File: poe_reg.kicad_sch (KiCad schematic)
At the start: 29 parts, among them T2 POE30P-50L, U5 MP6004GQ-P

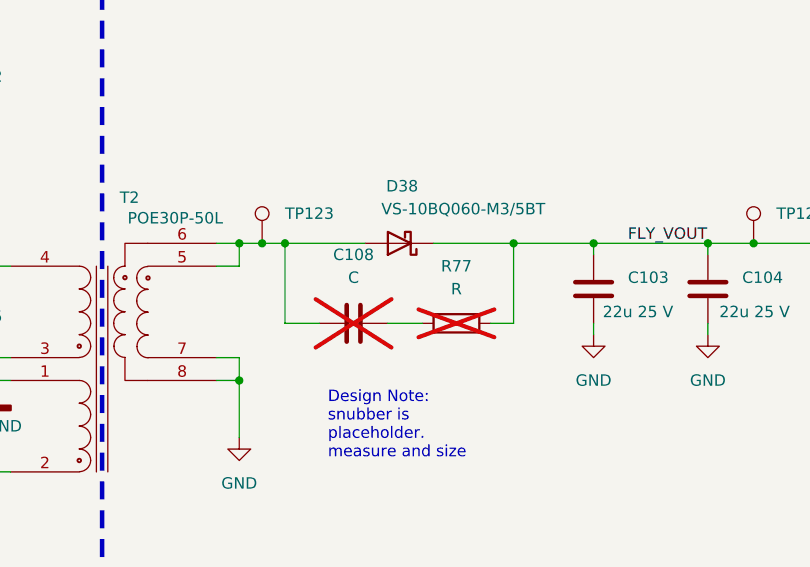
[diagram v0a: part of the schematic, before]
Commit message: did stuff, amongst others changed to op-amp input filter
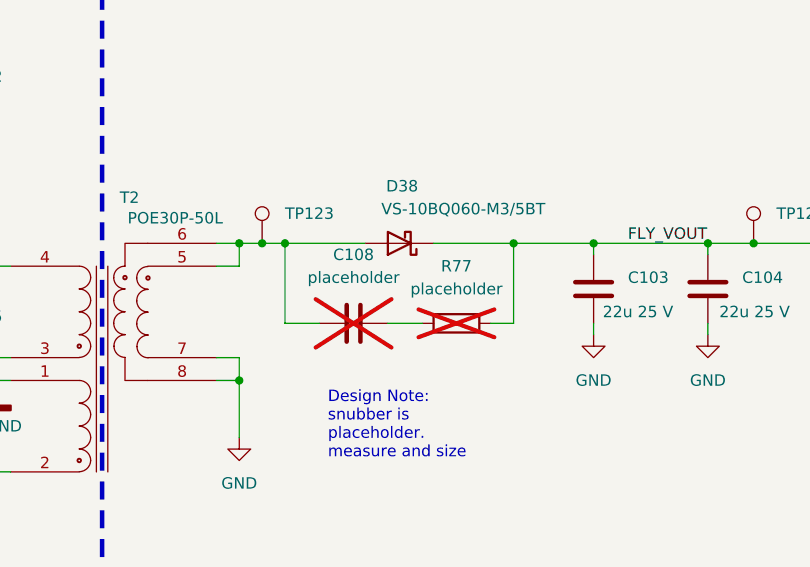
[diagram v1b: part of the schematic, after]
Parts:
- C108: value C -> placeholder
- D37: LCSC (none) -> C894760
- R77: value R -> placeholder

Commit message: did stuff
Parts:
- C102: LCSC (none) -> C2941944; LCSC Part (none) -> C2941944
- C106: LCSC (none) -> C170101; LCSC Basic/Pref (none) -> n; LCSC Part (none) -> C170101
- D80: value MMBZ5256ELT1G -> BZX84C30-7-F; LCSC (none) -> C151632; LCSC Basic/Pref (none) -> n; LCSC Part (none) -> C151632; LCSC missing x -> (none)
- R78: value 68k -> 150k; footprint Resistor_SMD:R_0402_1005Metric -> Resistor_SMD:R_0603_1608Metric; LCSC C36871 -> C22807; LCSC Part C36871 -> C22807
- R79: value 12k -> 24K; footprint Resistor_SMD:R_0402_1005Metric -> Resistor_SMD:R_0603_1608Metric; LCSC C25752 -> C23352; LCSC Part C25752 -> C23352
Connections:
- net +5.2V renamed +5.3V
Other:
- note removed: "TODO: Replace D80, not on LCSC"
- note removed: "TODO: recalc for 5.2 V"
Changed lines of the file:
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@@
 	(generator_version "10.0")
 	(paper "A3")
-	(text "TODO: recalc for 5.2 V"
+	(text "PoE Flyback Regulator"
 		(exclude_from_sim no)
-		(at 133.858 98.806 0)
+		(at 205.232 35.56 0)
 		(effects
 			(font
-				(size 1.27 1.27)
+				(size 12.7 12.7)
+				(thickness 1.5875)
 			)
 		)
 	)
-	(text "PoE Flyback Regulator"
+	(text "CAD Note:\n2kV isolation\n"
 		(exclude_from_sim no)
-		(at 150.622 25.4 0)
+		(at 210.312 92.456 0)
 		(effects
 			(font
-				(size 12.7 12.7)
-				(thickness 1.5875)
+				(size 1.27 1.27)
+				(color 255 0 3 1)
 			)
+			(justify left)
 		)
 	)
-	(text "TODO: Replace D80, not on LCSC"
+	(text_box "Design Note:\nD38 Vf = 0.42 V @ 1 A"
 		(exclude_from_sim no)
-		(at 76.454 120.396 0)
+		(at 260.35 113.03 0)
+		(size 26.67 5.9929)
+		(margins 0.9525 0.9525 0.9525 0.9525)
+		(stroke
+			(width -0.0001)
+			(type solid)
+		)
+		(fill
+			(type none)
+		)
 		(effects
 			(font
 				(size 1.27 1.27)
 			)
+			(justify left top)
 		)
 	)
-	(text "CAD Note:\n2kV isolation\n"
+	(text_box "Design Note:\n150k over 24k =>\n~5.321 V\nthere is significant inaccuracy\nworst case +/- ~0.5 V"
 		(exclude_from_sim no)
-		(at 210.312 92.456 0)
+		(at 180.34 177.8 0)
+		(size 27.94 20.3053)
+		(margins 0.9525 0.9525 0.9525 0.9525)
+		(stroke
+			(width -0.0001)
+			(type solid)
+		)
+		(fill
+			(type none)
+		)
 		(effects
 			(font
 				(size 1.27 1.27)
-				(color 255 0 3 1)
 			)
-			(justify left)
+			(justify left top)
 		)
 	)
@@
 		)
 	)
-	(text_box "Design Note:\nsnubber is placeholder.\nmeasure and size"
+	(text_box "Design Note:\nPOE30P-50L\n310uH (279uH Ipk)\n1.02 ohm pri 2.01 ohm bias 0.118 ohm sec\npri:sec = 1:0.28\npri:bias = 1:0.7"
 		(exclude_from_sim no)
-		(at 240.03 139.7 0)
-		(size 22.86 20.3053)
+		(at 220.98 96.52 0)
+		(size 45.72 14.1714)
 		(margins 0.9525 0.9525 0.9525 0.9525)
 		(stroke
@@
 		)
 	)
-	(text_box "Design Note:\nEN\n30 V Zener + 10k over 13k\n36.9 V rising\n32.3 V falling\n"
+	(text_box "Design Note:\nsnubber is placeholder.\nmeasure and size"
 		(exclude_from_sim no)
-		(at 68.58 156.21 0)
-		(size 22.86 14.1714)
+		(at 240.03 139.7 0)
+		(size 22.86 20.3053)
 		(margins 0.9525 0.9525 0.9525 0.9525)
 		(stroke
@@
 		)
 	)
-	(text_box "TODO:\nselect capacitors to chose footprints\n\nRCD diode"
+	(text_box "Design Note:\nEN\n30 V Zener + 10k over 13k\n36.9 V rising\n32.3 V falling\n"
 		(exclude_from_sim no)
-		(at 109.22 77.4847 0)
-		(size 22.86 20.3053)
+		(at 68.58 156.21 0)
+		(size 22.86 14.1714)
 		(margins 0.9525 0.9525 0.9525 0.9525)
 		(stroke
@@
 			)
 		)
-		(property "LCSC Basic/Pref" ""
+		(property "LCSC Basic/Pref" "n"
 			(at 124.46 115.57 0)
 			(hide yes)
@@
 			)
 		)
+		(property "LCSC" "C170101"
+			(at 124.46 115.57 0)
+			(hide yes)
+			(show_name no)
+			(do_not_autoplace no)
+			(effects
+				(font
+					(size 1.27 1.27)
+				)
+			)
+		)
+		(property "LCSC Part" "C170101"
+			(at 124.46 115.57 0)
+			(hide yes)
+			(show_name no)
+			(do_not_autoplace no)
+			(effects
+				(font
+					(size 1.27 1.27)
+				)
+			)
+		)
 		(pin "2"
 		)
@@
 			)
 		)
-		(property "Datasheet" "MP6004GQ-P"
+		(property "Datasheet" "https://www.monolithicpower.com/en/documentview/productdocument/index/version/2/document_type/Datasheet/lang/en/sku/MP6004/document_id/1864/"
 			(at 133.35 129.54 0)
 			(hide yes)
@@
 			)
 		)
+		(property "LCSC" "C2941944"
+			(at 190.5 114.3 0)
+			(hide yes)
+			(show_name no)
+			(do_not_autoplace no)
+			(effects
+				(font
+					(size 1.27 1.27)
+				)
+			)
+		)
+		(property "LCSC Part" "C2941944"
+			(at 190.5 114.3 0)
+			(hide yes)
+			(show_name no)
+			(do_not_autoplace no)
+			(effects
+				(font
+					(size 1.27 1.27)
+				)
+			)
+		)
 		(pin "2"
 		)
@@
 			)
 		)
-		(property "Value" "68k"
+		(property "Value" "150k"
 			(at 193.04 156.2099 0)
 			(show_name no)
@@
 			)
 		)
-		(property "Footprint" "Resistor_SMD:R_0402_1005Metric"
+		(property "Footprint" "Resistor_SMD:R_0603_1608Metric"
 			(at 188.722 154.94 90)
 			(hide yes)
@@
 			)
 		)
-		(property "LCSC" "C36871"
+		(property "LCSC" "C22807"
 			(at 190.5 154.94 0)
 			(hide yes)
@@
 			)
 		)
-		(property "LCSC Part" "C36871"
+		(property "LCSC Part" "C22807"
 			(at 190.5 154.94 0)
 			(hide yes)
@@
 			)
 		)
-		(property "Value" "MMBZ5256ELT1G"
+		(property "Value" "BZX84C30-7-F"
 			(at 77.724 129.032 90)
 			(show_name no)
@@
 			)
 		)
-		(property "LCSC Basic/Pref" ""
+		(property "LCSC Basic/Pref" "n"
 			(at 96.52 127 90)
 			(hide yes)
@@
 			)
 		)
-		(property "LCSC missing" "x"
+		(property "LCSC missing" ""
 			(at 96.52 127 90)
 			(hide yes)
@@
 			)
 		)
+		(property "LCSC" "C151632"
+			(at 96.52 127 90)
+			(hide yes)
+			(show_name no)
+			(do_not_autoplace no)
+			(effects
+				(font
+					(size 1.27 1.27)
+				)
+			)
+		)
+		(property "LCSC Part" "C151632"
+			(at 96.52 127 90)
+			(hide yes)
+			(show_name no)
+			(do_not_autoplace no)
+			(effects
+				(font
+					(size 1.27 1.27)
+				)
+			)
+		)
 		(pin "2"
 		)
@@
 			)
 		)
-		(property "Value" "12k"
+		(property "Value" "24K"
 			(at 193.04 166.3699 0)
 			(show_name no)
@@
 			)
 		)
-		(property "Footprint" "Resistor_SMD:R_0402_1005Metric"
+		(property "Footprint" "Resistor_SMD:R_0603_1608Metric"
 			(at 188.722 165.1 90)
 			(hide yes)
@@
 			)
 		)
-		(property "LCSC" "C25752"
+		(property "LCSC" "C23352"
 			(at 190.5 165.1 0)
 			(hide yes)
@@
 			)
 		)
-		(property "LCSC Part" "C25752"
+		(property "LCSC Part" "C23352"
 			(at 190.5 165.1 0)
 			(hide yes)
@@
 			)
 		)
-		(property "Value" "+5.2V"
+		(property "Value" "+5.3V"
 			(at 321.31 118.1099 0)
 			(show_name no)

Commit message: did stuff
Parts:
- U5: LCSC (none) -> C5800399; LCSC Basic/Pref (none) -> n; LCSC Part (none) -> C5800399
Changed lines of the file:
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@@
 			)
 		)
-		(property "LCSC Basic/Pref" ""
+		(property "LCSC Basic/Pref" "n"
 			(at 133.35 129.54 0)
 			(hide yes)
@@
 			(at 133.35 129.54 0)
 			(hide yes)
+			(show_name no)
+			(do_not_autoplace no)
+			(effects
+				(font
+					(size 1.27 1.27)
+				)
+			)
+		)
+		(property "LCSC" "C5800399"
+			(at 133.35 129.54 0)
+			(hide yes)
+			(show_name no)
+			(do_not_autoplace no)
+			(effects
+				(font
+					(size 1.27 1.27)
+				)
+			)
+		)
+		(property "LCSC Part" "C5800399"
+			(at 133.35 129.54 0)
+			(hide yes)

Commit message: fixed a lot of review comments
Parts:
- added R259: 10k, Resistor_SMD:R_0402_1005Metric, symbol Device:R
- C102: value 910p -> 1n 2kV; footprint Capacitor_SMD:C_0402_1005Metric -> Capacitor_SMD:C_1206_3216Metric; LCSC C2941944 -> C9196; LCSC Basic/Pref n -> y; LCSC Part C2941944 -> C9196; LCSC missing (none) -> n; MPN (none) -> 1206B102K202NT; Manufacturer (none) -> FH; TC (none) -> X7R
- C105: value 220u -> 220u 16V; LCSC (none) -> C2927909; LCSC Part (none) -> C2927909; LCSC missing (none) -> n; MPN (none) -> RVE220UF16V67RV0003; Manufacturer (none) -> KNSCHA
- C134: value 47u -> 47u 100V; LCSC (none) -> C87862; LCSC Part (none) -> C87862; MPN (none) -> RVT2A470M1010; Manufacturer (none) -> Honor Elec
- D37: now not fitted
- D80: value BZX84C30-7-F -> BZX84C30; footprint MMBZ5256ELT1G:SOT-23(1-3) -> C22379472:SOT-23-3_L2.9-W1.5-P2.0-LS2.5-BR; symbol Device:D_Zener -> C22379472:BZX84C30_C22379472; LCSC C151632 -> C22379472; LCSC Basic/Pref n -> y; LCSC Part C151632 -> C22379472
- R104: value 13k -> 33k; LCSC C22797 -> C25779; LCSC Part C22797 -> C25779
- R105: value 10k -> 33k; LCSC C25744 -> C25779; LCSC Basic/Pref x -> y; LCSC Part C25744 -> C25779; Tolerance (none) -> 1%
- R76: footprint Resistor_SMD:R_0402_1005Metric -> Resistor_SMD:R_0805_2012Metric; LCSC C25796 -> C17756; LCSC Basic/Pref x -> y; LCSC Part C25796 -> C17756; LCSC missing (none) -> n; MPN (none) -> 0805W8F5602T5E; Manufacturer (none) -> UNI-ROYAL; Power (none) -> 125 mW; Tolerance (none) -> 1
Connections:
- net FLY_EN: now also R259.1; no longer R104.1
- net VIN: now also D80.3 (K); no longer D80.1 (K)
- net at R105.1: now also D80.1 (A); no longer D80.2 (A)
- new net: R104.1, R259.2
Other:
- moved on the sheet: R104

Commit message: pre-changing properties
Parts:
- C108, D37, R77: now left out of the parts list
- R103: footprint Resistor_SMD:R_0603_1608Metric -> Resistor_SMD:R_0402_1005Metric; LCSC missing (none) -> n; MPN (none) -> 0402WGF3000TCE; Manufacturer (none) -> UNI-ROYAL(Uniroyal Elec); Power (none) -> UNI-ROYAL(Uniroyal Elec); Tolerance (none) -> 1%; Voltage (none) -> 50V
- R107: footprint Resistor_SMD:R_0603_1608Metric -> Resistor_SMD:R_0402_1005Metric; LCSC missing (none) -> n; MPN (none) -> 0402WGF2000TCE; Manufacturer (none) -> UNI-ROYAL(Uniroyal Elec); Power (none) -> 62.5mW; Tolerance (none) -> 1%; Voltage (none) -> 50V
- R259: LCSC Basic/Pref x -> y; LCSC missing (none) -> n; MPN (none) -> 0402WGF1002TCE; Manufacturer (none) -> UNI-ROYAL; Power (none) -> 62.5mW; Tolerance (none) -> 1%
